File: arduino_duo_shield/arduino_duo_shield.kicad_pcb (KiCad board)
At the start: 2 copper layers, 102.1 x 119.4 mm, 76 parts, among them J2 EStop, J3 Motor_Control, J4 Limit_Switches, J5 inverter_freq, J6 inverter_cmd, J8 inverter_power, J9 Motor_Control_Mirror, K2 JQC-3F, K3 JQC-3F, P10 Digital, P11 PWM, P12 PWM, P13 Communication, P7 Power, P8 Analog, P9 Analog, Q3 2N7000, Q4 BS250, Q5 2N7000, Q6 2N7000, SW1 SW_Push, U1 4504, U2 4504, U3 LM358, U4 74HC14, U6 74HC14, U7 PC817, U8 PC817, U9 PC817

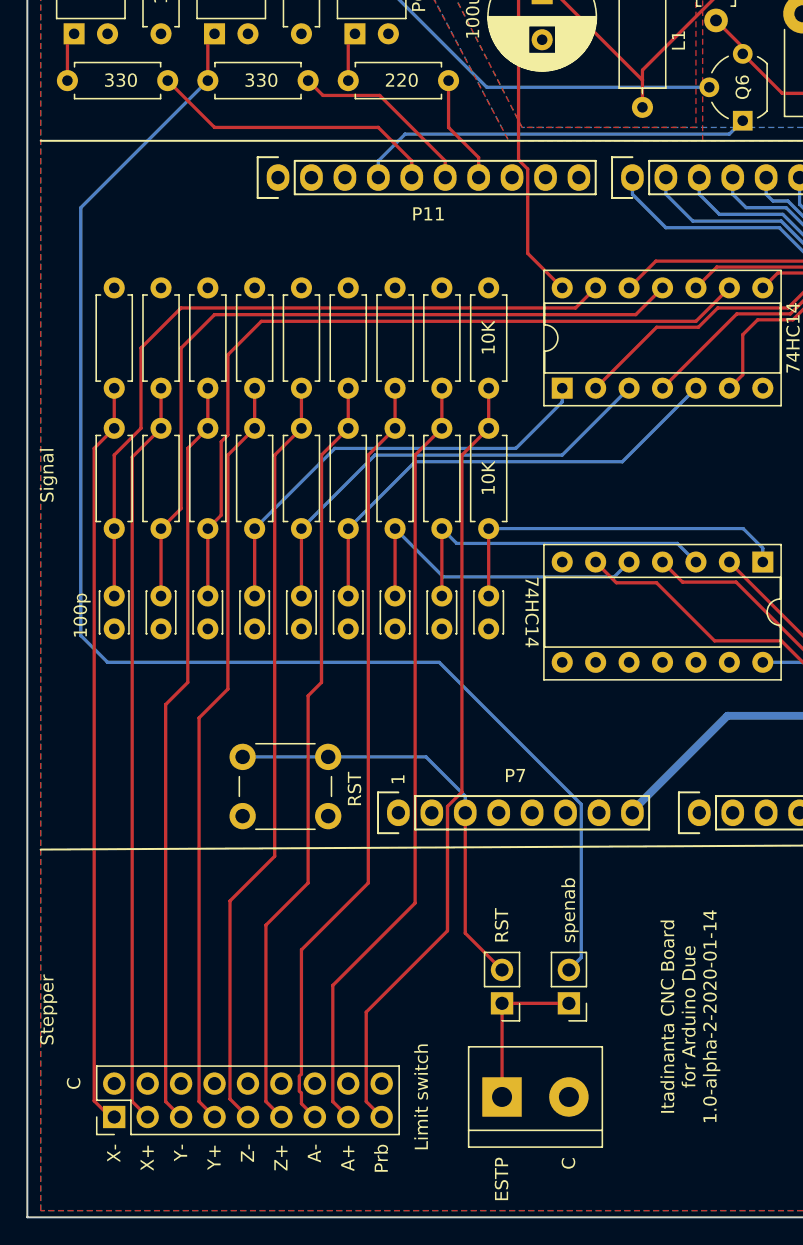
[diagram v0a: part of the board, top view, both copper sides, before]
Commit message: Add support for 24LC16 EEPROM
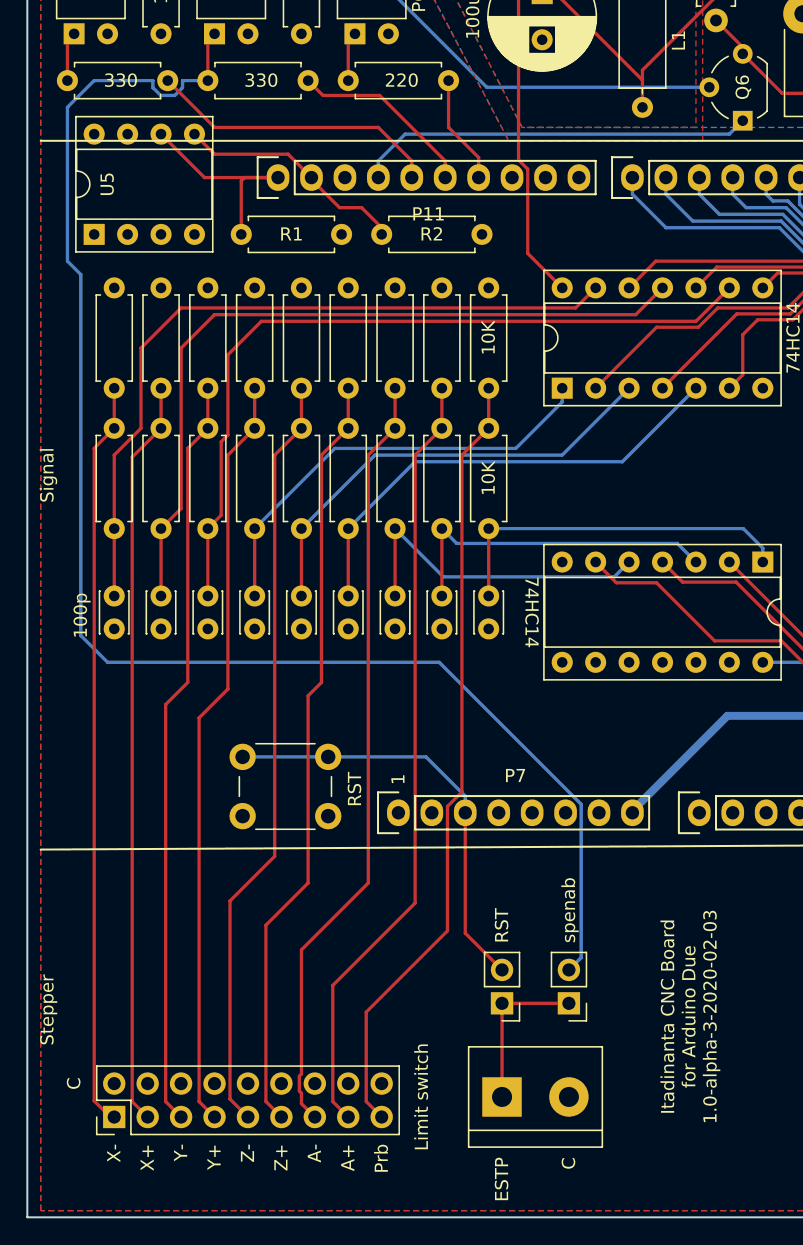
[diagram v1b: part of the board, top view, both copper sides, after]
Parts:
- added R1: 1K5, Resistor_THT:R_Axial_DIN0207_L6.3mm_D2.5mm_P7.62mm_Horizontal, F.Cu at (119.4, 75.2)
- added R2: 1K5, Resistor_THT:R_Axial_DIN0207_L6.3mm_D2.5mm_P7.62mm_Horizontal, F.Cu at (137.7, 75.2)
- added U5: 24LC16, Package_DIP:DIP-8_W7.62mm_Socket, F.Cu at (108.2, 75.2)
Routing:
- net /SDA: track 0.00 -> 17.8 mm
- net /SCL: track 0.00 -> 17.2 mm
- net /Spindle_VFD_Control/ext_estop: track 106.2 -> 113.7 mm
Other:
- board text added: "Itadinanta CNC Board for Arduino Due 1.0-alpha-3-2020-02-03"
- board text removed: "Itadinanta CNC Board for Arduino Due 1.0-alpha-2-2020-01-14"

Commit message: Tidy up, generate plots for JLCPCB, alpha 4
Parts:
- moved R2 13.4 mm to (126.0, 81.8), turned to 90 degrees
- moved C8 7.27 mm to (145.3, 63.5), turned to 180 degrees
- moved U5 6.43 mm to (110.2, 81.3)
- moved R11 5.59 mm to (113.3, 92.5)
- moved R13 5.59 mm to (109.7, 92.5)
- moved R19 5.59 mm to (138.2, 92.5)
- moved R27 5.59 mm to (134.6, 92.5)
- moved R29 5.59 mm to (131.1, 92.5)
- moved R3 5.59 mm to (127.5, 92.5)
- moved R5 5.59 mm to (124.0, 92.5)
- moved R7 5.59 mm to (120.4, 92.5)
- moved R9 5.59 mm to (116.8, 92.5)
- moved R10 5.08 mm to (116.8, 102.6)
- moved R12 5.08 mm to (113.3, 102.6)
- moved R14 5.08 mm to (109.7, 102.6)
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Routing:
- net /SCL: track 17.2 -> 10.9 mm
- net Net-(C4-Pad2): track 33.5 -> 39.3 mm
- net /Debounce_x6/SWXmin+: track 56.8 -> 51.0 mm
- net /Debounce_x6/SWZmin+: track 58.2 -> 52.6 mm
- net /Debounce_x6/SWZmax+: track 58.4 -> 52.9 mm
- net /Debounce_x6/SWProbe+: track 59.7 -> 54.1 mm
- net /Debounce_x6/SWAmax+: track 59.3 -> 53.7 mm
- net /Debounce_x6/SWYmin+: track 57.2 -> 51.6 mm
- net /Debounce_x6/SWYmax+: track 57.6 -> 52.0 mm
- net /Debounce_x6/SWXmax+: track 56.8 -> 51.2 mm
- net /Debounce_x6/SWAmin+: track 58.9 -> 53.3 mm
- net Net-(C3-Pad2): track 34.4 -> 38.8 mm
- net Net-(C2-Pad2): track 36.0 -> 40.4 mm
- net /Spindle_VFD_Control/inverter_frequency_raw_10V: track 74.6 -> 70.3 mm
- net /SDA: track 17.8 -> 14.4 mm
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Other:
- board text added: "Itadinanta CNC Board for Arduino Due 1.0-alpha-4-2020-02-06"
- board text removed: "Itadinanta CNC Board for Arduino Due 1.0-alpha-3-2020-02-03"
